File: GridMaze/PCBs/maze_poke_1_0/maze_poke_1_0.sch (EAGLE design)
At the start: 16 parts

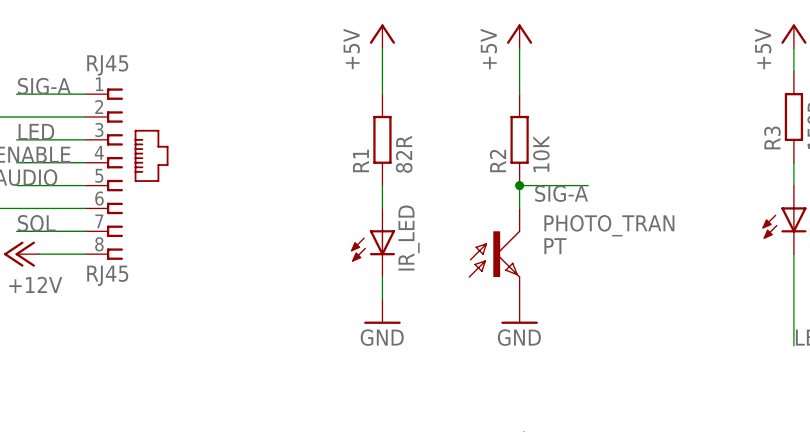
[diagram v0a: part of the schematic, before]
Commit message: Changes to 3x3 GridMaze hardware:
- Rather than seperate tall and short variants there is now a single intermediate height version of the maze.

- IR illumination is now provided by IR module PCBs which connect to the maze hub board using a Molex Micro-Fit cable and can be daisy chained.

- Reduced Poke IR beam current from 50mA to 40mA.
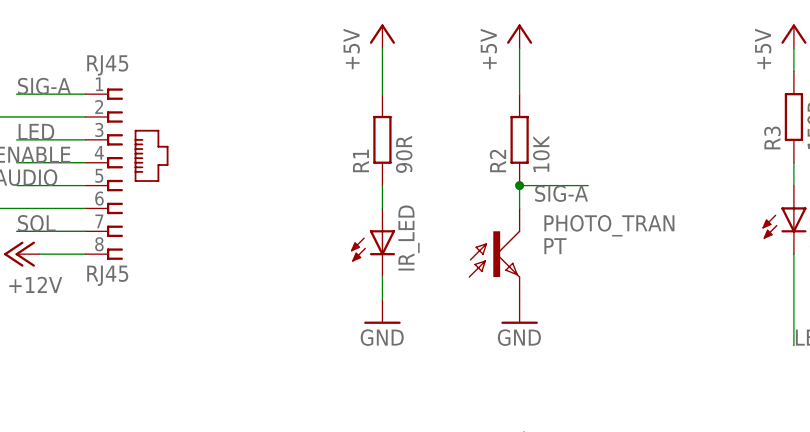
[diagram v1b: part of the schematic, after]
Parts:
- R1: value 82R -> 90R
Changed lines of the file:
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@@
 </classes>
 <parts>
-<part name="R1" library="resistor" deviceset="R-EU_" device="R0805" value="82R"/>
+<part name="R1" library="resistor" deviceset="R-EU_" device="R0805" value="90R"/>
 <part name="R3" library="resistor" deviceset="R-EU_" device="M0805" value="150R"/>
 <part name="LED" library="led" deviceset="LED" device="SML0805"/>
